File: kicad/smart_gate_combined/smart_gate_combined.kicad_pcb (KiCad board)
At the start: 2 copper layers, 201.7 x 119.6 mm, 31 parts

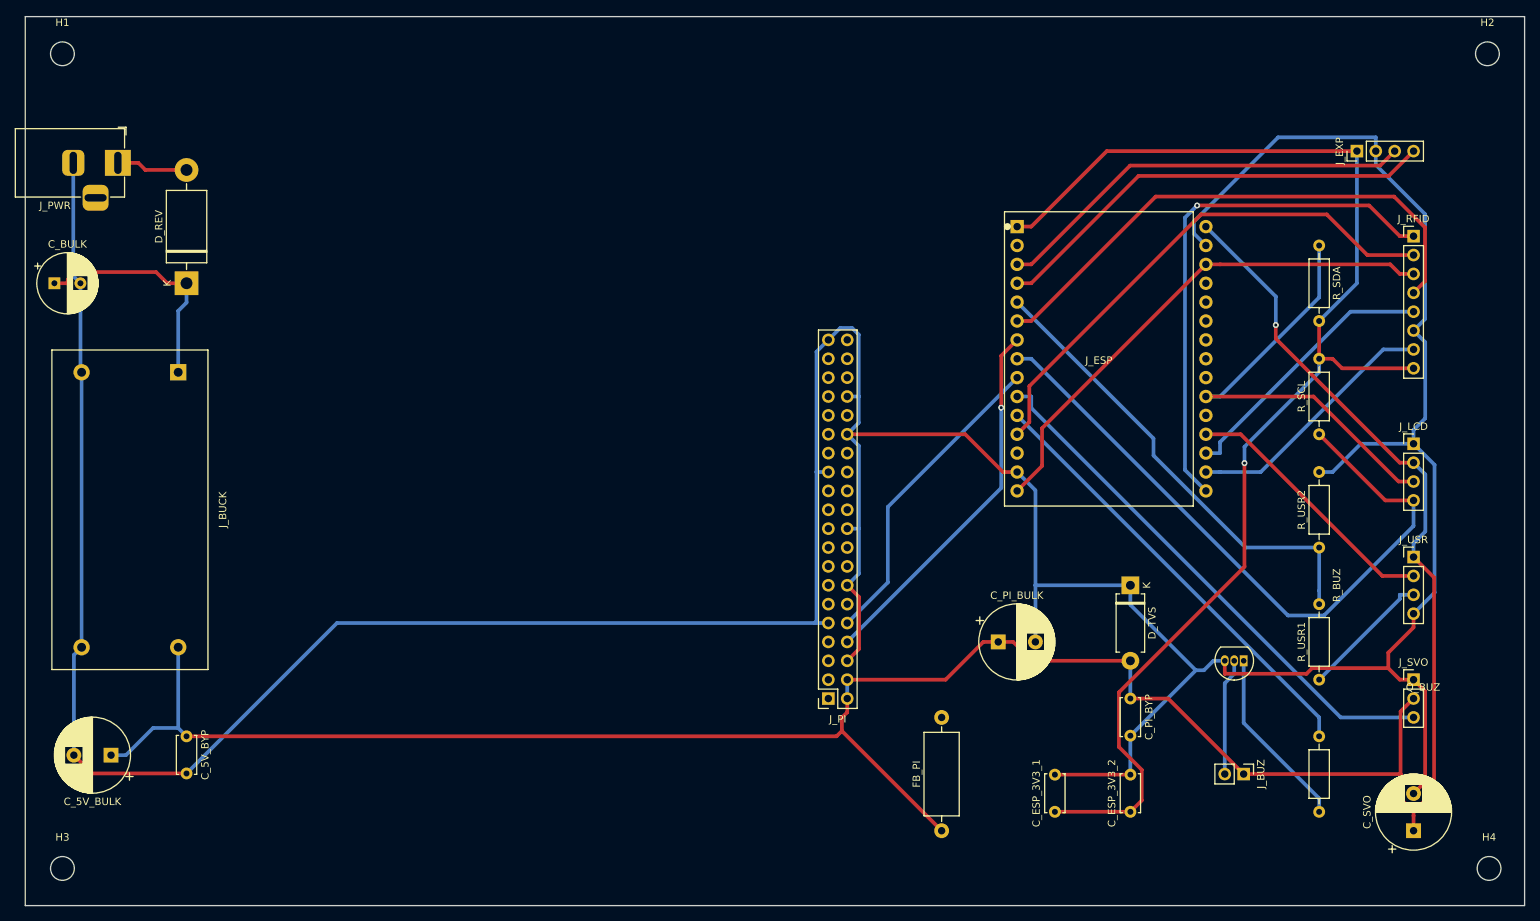
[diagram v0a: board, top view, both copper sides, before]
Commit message: feat(kicad): GND copper pour on both F.Cu and B.Cu layers
add_gnd_pour.py now adds two GND zones (one per copper layer), both
fitting the Edge.Cuts geometry with 0.5mm margin. Removed leftover
single-zone code from earlier single-layer version.

Final PCB state:
- 238 signal tracks @ 0.5mm (F.Cu 112 + B.Cu 126)
- 4 vias
- 2 GND copper pour zones (F.Cu + B.Cu)
- 31 footprints
- DRC: 0 errors, 0 unconnected pads, 6 cosmetic silk warnings

Ready for gerber export and fab.

Co-Authored-By: Claude Opus 4.7 <noreply@anthropic.com>
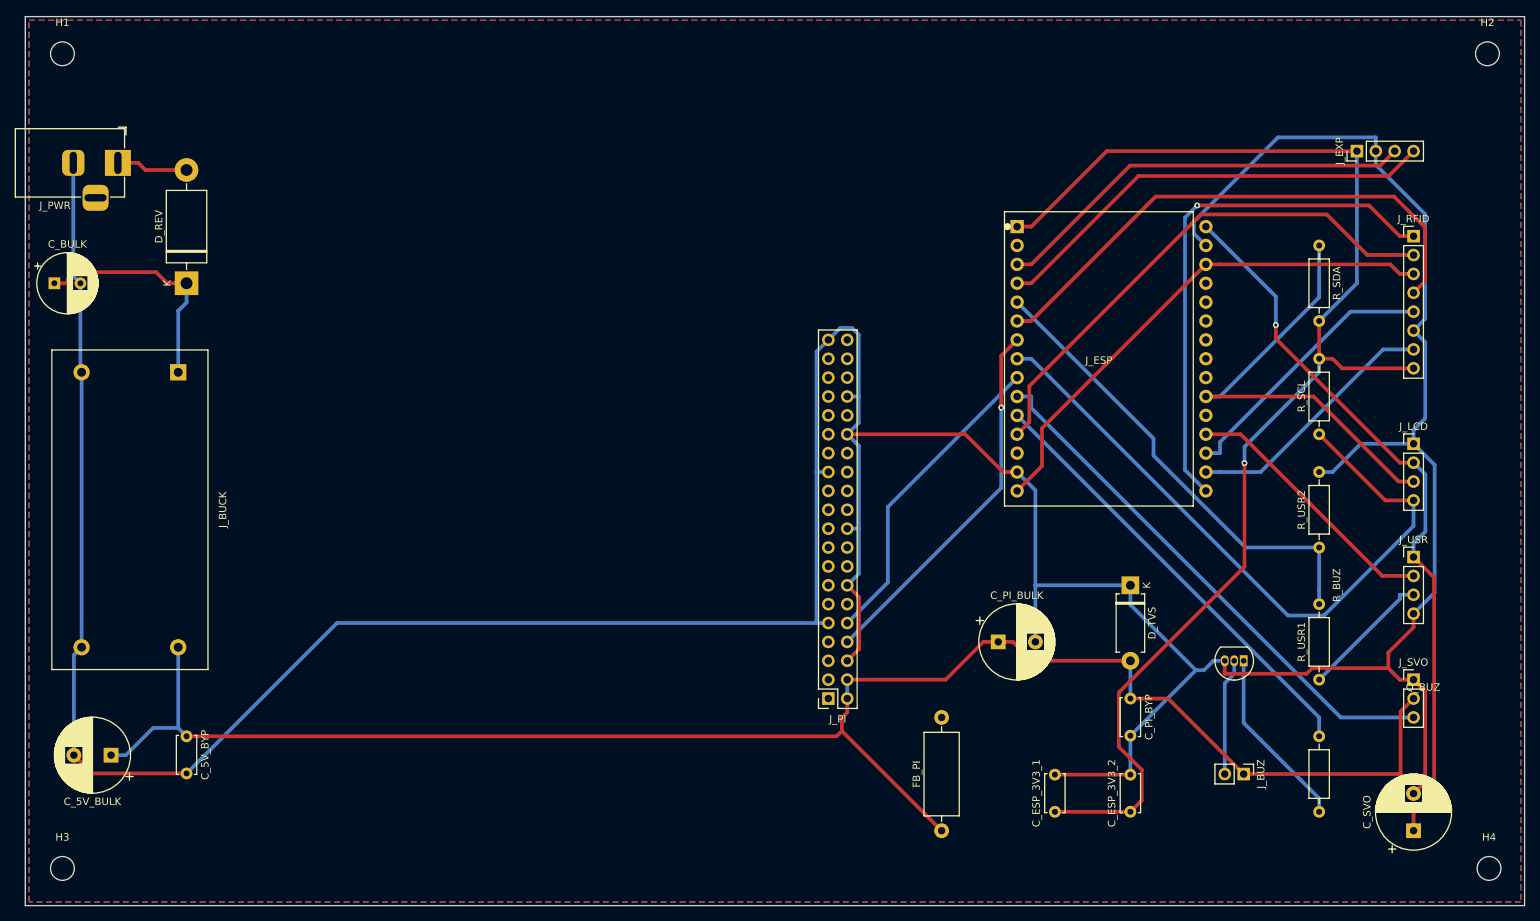
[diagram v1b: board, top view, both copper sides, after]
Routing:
- added copper zone on B.Cu, net GND
- added copper zone on F.Cu, net GND
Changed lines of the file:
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@@
   (segment (start 207.64 68.58) (end 207.64 70.1237) (width 0.5) (layer "B.Cu") (net 25))
   (segment (start 205.74 68.58) (end 207.64 68.58) (width 0.5) (layer "B.Cu") (net 25))
+  (zone (net 7) (net_name "GND") (layer "F.Cu") (hatch edge 0.508)
+    (connect_pads (clearance 0.25))
+    (min_thickness 0.25) (filled_areas_thickness no)
+    (fill yes (thermal_gap 0.5) (thermal_bridge_width 0.5))
+    (polygon
+      (pts
+        (xy 72.78 17.9625)
+        (xy 273.52 17.9625)
+        (xy 273.52 136.58)
+        (xy 72.78 136.58)
+      )
+    )
+  )
+  (zone (net 7) (net_name "GND") (layer "B.Cu") (hatch edge 0.508)
+    (connect_pads (clearance 0.25))
+    (min_thickness 0.25) (filled_areas_thickness no)
+    (fill yes (thermal_gap 0.5) (thermal_bridge_width 0.5))
+    (polygon
+      (pts
+        (xy 72.78 17.9625)
+        (xy 273.52 17.9625)
+        (xy 273.52 136.58)
+        (xy 72.78 136.58)
+      )
+    )
+  )
 )
